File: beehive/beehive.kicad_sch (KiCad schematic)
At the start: 23 parts, among them J1 M05PTH, Q1 MMBT4403, U1 ESP32-S3-WROOM-1U, U2 HX711, U3 ADXL362

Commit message: added custom library submodule
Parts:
- C1, C2, C3, C4, C5: footprint SparkFun_HX711_Load_Cell:0603-CAP -> Board_SparkFun_HX711_Load_Cell:0603-CAP
- C6, C7: footprint SparkFun_HX711_Load_Cell:1210 -> Board_SparkFun_HX711_Load_Cell:1210
- C8: footprint ADXL362 BOB v01:0402-CAP -> Board_ADXL362_BOB_v01:0402-CAP
- J1, JP4: footprint SparkFun_HX711_Load_Cell:1X05 -> Board_SparkFun_HX711_Load_Cell:1X05
- JP1: footprint ADXL362 BOB v01:1X04 -> Board_ADXL362_BOB_v01:1X04
- JP2: footprint SparkFun_HX711_Load_Cell:1X02 -> Board_SparkFun_HX711_Load_Cell:1X02
- L1: footprint SparkFun_HX711_Load_Cell:0805 -> Board_SparkFun_HX711_Load_Cell:0805
- Q1: footprint SparkFun_HX711_Load_Cell:SOT23-3 -> Board_SparkFun_HX711_Load_Cell:SOT23-3
- R1, R2, R3, R4, R5: footprint SparkFun_HX711_Load_Cell:0603-RES -> Board_SparkFun_HX711_Load_Cell:0603-RES
- SJ2: footprint SparkFun_HX711_Load_Cell:PAD-JUMPER-2-NC_BY_TRACE_YES_SILK -> Board_SparkFun_HX711_Load_Cell:PAD-JUMPER-2-NC_BY_TRACE_YES_SILK
- U1: footprint ESP32:XCVR_ESP32-S3-WROOM-1U -> ESP32-S3-WROOM-1:XCVR_ESP32-S3-WROOM-1U
- U3: footprint adxl362:LGA-16-3X2.5 -> ADXL362:LGA-16-3X2.5
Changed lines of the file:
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@@
 			)
 		)
-		(property "Footprint" "SparkFun_HX711_Load_Cell:1X02"
+		(property "Footprint" "Board_SparkFun_HX711_Load_Cell:1X02"
 			(at 217.17 74.93 0)
 			(effects
@@
 			)
 		)
-		(property "Footprint" "SparkFun_HX711_Load_Cell:0603-CAP"
+		(property "Footprint" "Board_SparkFun_HX711_Load_Cell:0603-CAP"
 			(at 250.19 29.21 0)
 			(effects
@@
 			)
 		)
-		(property "Footprint" "SparkFun_HX711_Load_Cell:0805"
+		(property "Footprint" "Board_SparkFun_HX711_Load_Cell:0805"
 			(at 273.05 49.53 0)
 			(effects
@@
 			)
 		)
-		(property "Footprint" "SparkFun_HX711_Load_Cell:0603-CAP"
+		(property "Footprint" "Board_SparkFun_HX711_Load_Cell:0603-CAP"
 			(at 247.65 57.15 0)
 			(effects
@@
 			)
 		)
-		(property "Footprint" "SparkFun_HX711_Load_Cell:SOT23-3"
+		(property "Footprint" "Board_SparkFun_HX711_Load_Cell:SOT23-3"
 			(at 293.37 41.91 0)
 			(effects
@@
 			)
 		)
-		(property "Footprint" "SparkFun_HX711_Load_Cell:0603-RES"
+		(property "Footprint" "Board_SparkFun_HX711_Load_Cell:0603-RES"
 			(at 285.75 72.39 0)
 			(effects
@@
 			)
 		)
-		(property "Footprint" "SparkFun_HX711_Load_Cell:0603-CAP"
+		(property "Footprint" "Board_SparkFun_HX711_Load_Cell:0603-CAP"
 			(at 295.91 97.79 0)
 			(effects
@@
 			)
 		)
-		(property "Footprint" "SparkFun_HX711_Load_Cell:1X05"
+		(property "Footprint" "Board_SparkFun_HX711_Load_Cell:1X05"
 			(at 217.17 54.61 0)
 			(effects
@@
 			)
 		)
-		(property "Footprint" "SparkFun_HX711_Load_Cell:0603-RES"
+		(property "Footprint" "Board_SparkFun_HX711_Load_Cell:0603-RES"
 			(at 285.75 57.15 0)
 			(effects
@@
 			)
 		)
-		(property "Footprint" "ADXL362 BOB v01:0402-CAP"
+		(property "Footprint" "Board_ADXL362_BOB_v01:0402-CAP"
 			(at 353.06 201.93 0)
 			(effects
@@
 			)
 		)
-		(property "Footprint" "SparkFun_HX711_Load_Cell:0603-RES"
+		(property "Footprint" "Board_SparkFun_HX711_Load_Cell:0603-RES"
 			(at 288.29 102.87 0)
 			(effects
@@
 			)
 		)
-		(property "Footprint" "SparkFun_HX711_Load_Cell:0603-RES"
+		(property "Footprint" "Board_SparkFun_HX711_Load_Cell:0603-RES"
 			(at 288.29 90.17 0)
 			(effects
@@
 			)
 		)
-		(property "Footprint" "ESP32:XCVR_ESP32-S3-WROOM-1U"
+		(property "Footprint" "ESP32-S3-WROOM-1:XCVR_ESP32-S3-WROOM-1U"
 			(at 45.72 74.93 0)
 			(effects
@@
 			)
 		)
-		(property "Footprint" "SparkFun_HX711_Load_Cell:0603-RES"
+		(property "Footprint" "Board_SparkFun_HX711_Load_Cell:0603-RES"
 			(at 351.79 39.37 0)
 			(effects
@@
 			)
 		)
-		(property "Footprint" "SparkFun_HX711_Load_Cell:0603-CAP"
+		(property "Footprint" "Board_SparkFun_HX711_Load_Cell:0603-CAP"
 			(at 298.45 80.01 0)
 			(effects
@@
 			)
 		)
-		(property "Footprint" "ADXL362 BOB v01:1X04"
+		(property "Footprint" "Board_ADXL362_BOB_v01:1X04"
 			(at 312.42 161.29 0)
 			(effects
@@
 			)
 		)
-		(property "Footprint" "SparkFun_HX711_Load_Cell:0603-CAP"
+		(property "Footprint" "Board_SparkFun_HX711_Load_Cell:0603-CAP"
 			(at 262.89 29.21 0)
 			(effects
@@
 			)
 		)
-		(property "Footprint" "SparkFun_HX711_Load_Cell:1210"
+		(property "Footprint" "Board_SparkFun_HX711_Load_Cell:1210"
 			(at 278.13 29.21 0)
 			(effects
@@
 			)
 		)
-		(property "Footprint" "SparkFun_HX711_Load_Cell:1X05"
+		(property "Footprint" "Board_SparkFun_HX711_Load_Cell:1X05"
 			(at 379.73 69.85 0)
 			(effects
@@
 			)
 		)
-		(property "Footprint" "adxl362:LGA-16-3X2.5"
+		(property "Footprint" "ADXL362:LGA-16-3X2.5"
 			(at 316.23 196.85 0)
 			(effects
@@
 			)
 		)
-		(property "Footprint" "SparkFun_HX711_Load_Cell:1210"
+		(property "Footprint" "Board_SparkFun_HX711_Load_Cell:1210"
 			(at 257.81 57.15 0)
 			(effects
@@
 			)
 		)
-		(property "Footprint" "SparkFun_HX711_Load_Cell:PAD-JUMPER-2-NC_BY_TRACE_YES_SILK"
+		(property "Footprint" "Board_SparkFun_HX711_Load_Cell:PAD-JUMPER-2-NC_BY_TRACE_YES_SILK"
 			(at 351.79 54.61 0)
 			(effects

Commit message: TP5100 and ESP32 remaining
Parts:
- removed JP1: M04PTH, Board_ADXL362_BOB_v01:1X04, symbol ADXL362 BOB v01-eagle-import:M04PTH
- added C10, C9: 10uF/25V, Capacitor_SMD:C_0603_1608Metric_Pad1.08x0.95mm_HandSolder, symbol Device:C
- added C11: 0.1uF, symbol Device:C
- added C12: 3.9nF, symbol Device:C
- added C13, C14: 22uF/6.3V, symbol Device:C
- added C15: 10nF, symbol Device:C
- added C16, C17: 1uF, symbol Device:C
- added IC1: MP2307, MP2307:SO8-TH, symbol MP2307:MP2307
- added J2, J3: Conn_01x04_Pin, Connector_JST:JST_XH_B4B-XH-A_1x04_P2.50mm_Vertical, symbol Connector:Conn_01x04_Pin
- added J4: Conn_01x07_Socket, Connector_JST:JST_XH_B7B-XH-A_1x07_P2.50mm_Vertical, symbol Connector:Conn_01x07_Socket
- added J5: Conn_01x04_Pin, symbol Connector:Conn_01x04_Pin
- added J6: Screw_Terminal_01x07, symbol Connector:Screw_Terminal_01x07
- added J7, J8: Conn_01x03_Pin, symbol Connector:Conn_01x03_Pin
- added L2: 10uH/4A, symbol Device:L
- added R6: 100k, symbol Device:R_US
- added R7: 6.8k, symbol Device:R_US
- added R8: 28.7k/1%, symbol Device:R_US
- added R9: 10k/1%, symbol Device:R_US
- added U5: TP5100, TP5100:QFN65P400X400X90-17N, symbol TP5100:TP5100
- added U6: MCP1700x-330xxTT, Package_TO_SOT_SMD:SOT-23, symbol Regulator_Linear:MCP1700x-330xxTT
- C1, C2, C3, C4, C5: symbol SparkFun_HX711_Load_Cell-eagle-import:0.1UF-25V-5%(0603) -> Board_SparkFun_HX711_Load_Cell:0.1UF-25V-5%(0603)
- C8: value .1uF -> 0.1uF; symbol ADXL362 BOB v01-eagle-import:CAP0402-CAP -> Board_SparkFun_HX711_Load_Cell:0.1UF-25V-5%(0603)
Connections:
- net 3.3V is gone; now on net +3.3V: C8.2
- net GND: now also U3.P$12 (GND), U3.P$13 (GND), U3.P$16 (GND), C10.2, C11.2, C13.2, C14.1, C16.2, C17.2, C9.2, IC1.4 (GND), J2.2 (Pin_2), J4.2 (Pin_2), J5.2 (Pin_2), J8.1 (Pin_1), L2.2, R7.1, R9.2
- net SCK: now also J4.4 (Pin_4), J7.3 (Pin_3)
- net +3.3V: now reaches U3.P$1 (VDDIO)
- net +3.3V: now also U3.P$14 (VS), C16.1, J2.1 (Pin_1), J4.1 (Pin_1), J5.1 (Pin_1), J8.2 (Pin_2), U6.2 (VO)
- net at U3.P$11 (INT1): now also J2.3 (Pin_3)
- net at U3.P$4 (SCLK): now also J3.4 (Pin_4)
- net at U3.P$6 (MOSI): now also J3.3 (Pin_3)
- net at U3.P$7 (MISO): now also J3.2 (Pin_2)
- net at U3.P$8 (~{CS}): now also J3.1 (Pin_1)
- net at U3.P$9 (INT2): now also J2.4 (Pin_4)
- new net: C12.1, IC1.6 (COMP)
- new net: C12.2, R7.2
- new net: C13.1, C14.2, R8.1
- new net: C15.2, C17.1, IC1.3 (SW), L2.1, U6.3 (VI)
- new net: C11.1, IC1.8 (SS)
- new net: C15.1, IC1.1 (BS)
- new net: IC1.5 (FB), R8.2, R9.1
- new net: IC1.7 (EN), R6.2
- new net: U5.1 (VIN), U5.16 (VIN), U5.4 (VIN), U5.5 (VIN)
- new net: U5.2 (LX), U5.3 (LX)
- new net +BATT: C10.1, C9.1, IC1.2 (IN), R6.1
- new net SCL: J4.6 (Pin_6), J5.3 (Pin_3)
- new net SD: J4.3 (Pin_3), J8.3 (Pin_3)
- new net SDA: J4.7 (Pin_7), J5.4 (Pin_4)
- new net WS: J4.5 (Pin_5), J7.2 (Pin_2)
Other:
- note added: "BME280"
- note added: "INMP441"
- moved on the sheet: C8, U1, U3

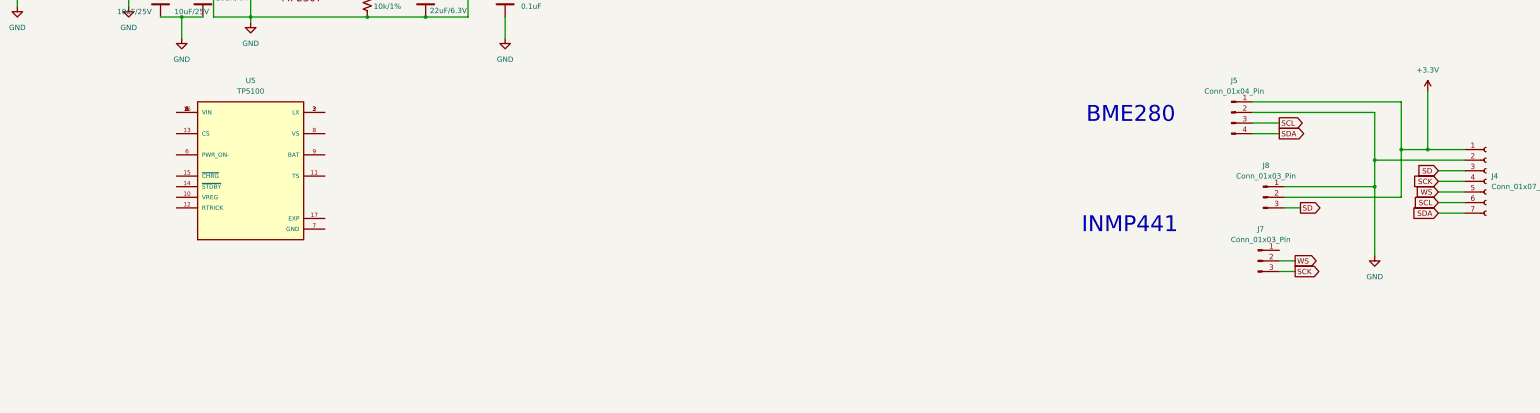
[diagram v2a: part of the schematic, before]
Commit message: change connection from the sensor block
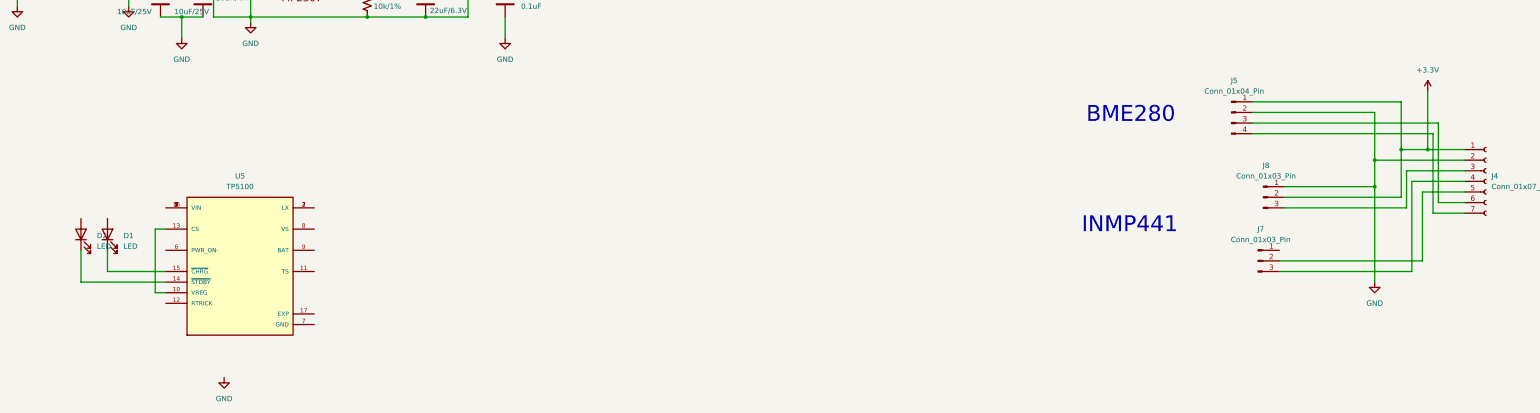
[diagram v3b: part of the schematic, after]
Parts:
- added D1, D2: LED, symbol Device:LED
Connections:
- net SCK: no longer J4.4 (Pin_4), J7.3 (Pin_3)
- net at U5.10 (VREG): now also U5.13 (CS)
- net at U5.14 (~{STDBY}): now also D2.1 (K)
- net at U5.15 (~{CHRG}): now also D1.1 (K)
- net SCL: no longer names the net of J4.6 (Pin_6), J5.3 (Pin_3)
- net SD: no longer names the net of J4.3 (Pin_3), J8.3 (Pin_3)
- net SDA: no longer names the net of J4.7 (Pin_7), J5.4 (Pin_4)
- net WS: no longer names the net of J4.5 (Pin_5), J7.2 (Pin_2)
- new net: J4.4 (Pin_4), J7.3 (Pin_3)
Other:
- moved on the sheet: U5

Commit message: 123
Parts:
- removed J1: M05PTH, Board_SparkFun_HX711_Load_Cell:1X05, symbol SparkFun_HX711_Load_Cell-eagle-import:M05PTH
- removed J3: Conn_01x04_Pin, Connector_JST:JST_XH_B4B-XH-A_1x04_P2.50mm_Vertical, symbol Connector:Conn_01x04_Pin
- added BT1: Battery, symbol Device:Battery
- added C18, C19, C22, C24, C26, C27, C28: 0.1uF, symbol Device:C
- added C20, C21, C23, C25: 10uF, Capacitor_SMD:C_0603_1608Metric_Pad1.08x0.95mm_HandSolder, symbol Device:C
- added J9: USB_C_Receptacle_USB2.0_16P, symbol Connector:USB_C_Receptacle_USB2.0_16P
- added L3: 22uH/2A, symbol Device:L
- added R10: 1k, symbol Device:R_US
- added R11: 0.1, symbol Device:R_US
- added R12: 10k, Board_SparkFun_HX711_Load_Cell:0603-RES, symbol SparkFun_HX711_Load_Cell-eagle-import:20KOHM1/10W1%(0603)
- added R13: 100, Board_SparkFun_HX711_Load_Cell:0603-RES, symbol SparkFun_HX711_Load_Cell-eagle-import:20KOHM1/10W1%(0603)
- added R14, R15: 5.1k, Resistor_SMD:R_0805_2012Metric_Pad1.20x1.40mm_HandSolder, symbol SparkFun_HX711_Load_Cell-eagle-import:20KOHM1/10W1%(0603)
- added R16, R17: 4.7k, Board_SparkFun_HX711_Load_Cell:0603-RES, symbol SparkFun_HX711_Load_Cell-eagle-import:20KOHM1/10W1%(0603)
- added SW1, SW2: SW_Push, symbol Switch:SW_Push
- D1: value LED -> LED red
- D2: value LED -> LED green
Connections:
- net DAT is gone; now on net IO4_DOUT: U2.12 (DOUT)
- net SCK is gone; now on net IO3_PD_SCK: U2.11 (PD_SCK)
- net +3.3V: now also J6.1 (Pin_1), U1.2 (3V3), C25.1, C26.1, R12.1, R16.2, R17.2
- net GND: now also J6.2 (Pin_2), U1.1 (GND), U1.40 (GND), U1.41_1 (GND), U1.41_2 (GND), U1.41_3 (GND), U1.41_4 (GND), U1.41_5 (GND), U1.41_6 (GND), U1.41_7 (GND), U1.41_8 (GND), U1.41_9 (GND), U5.11 (TS), U5.17 (EXP), U5.7 (GND), C18.2, C19.2, C20.2, C21.2, C22.2, C23.2, C24.2, C25.2, C26.2, C27.2, C28.2, J9.A1 (GND), J9.A12 (GND), J9.B1 (GND), J9.B12 (GND), J9.S1 (SHIELD), R14.2, R15.2, SW1.2, SW2.2
- net IO10_CS: now reaches U3.P$8 (~{CS})
- net IO10_CS: now also U1.18 (IO10)
- net IO13_MISO: now reaches U3.P$7 (MISO)
- net IO13_MISO: now also U1.21 (IO13)
- net IO11_MOSI: now reaches U3.P$6 (MOSI)
- net IO11_MOSI: now also U1.19 (IO11)
- net IO12_SCLK: now reaches U3.P$4 (SCLK)
- net IO12_SCLK: now also U1.20 (IO12)
- net INMP_SD: now reaches J4.3 (Pin_3), J8.3 (Pin_3)
- net INMP_WS: now reaches J4.5 (Pin_5), J7.2 (Pin_2)
- net INMP_SCK: now reaches J4.4 (Pin_4), J7.3 (Pin_3)
- net at D2.2 (A): now also D1.2 (A), R10.2
- net IO8_SDA: now reaches U1.12 (IO8)
- net IO8_SDA: now also J6.7 (Pin_7), R17.1
- net D-: now reaches U1.13 (IO19)
- net D-: now also J9.A7 (D-), J9.B7 (D-)
- net D+: now reaches U1.14 (IO20)
- net D+: now also J9.A6 (D+), J9.B6 (D+)
- net IO3_PD_SCK: now reaches U1.15 (IO3)
- net IO9_SCL: now reaches U1.17 (IO9)
- net IO9_SCL: now also J6.6 (Pin_6), R16.1
- net BOOT: now reaches U1.27 (IO0)
- net BOOT: now also R13.1
- net EN: now reaches U1.3 (EN)
- net EN: now also C27.1, C28.1, R12.2, SW1.1
- net IO4_DOUT: now reaches U1.4 (IO4)
- net IO5_SD: now reaches U1.5 (IO5)
- net IO5_SD: now also J6.3 (Pin_3)
- net IO6_WS: now reaches U1.6 (IO6)
- net IO6_WS: now also J6.4 (Pin_4)
- net IO7_SCK: now reaches U1.7 (IO7)
- net IO7_SCK: now also J6.5 (Pin_5)
- net +12V: now reaches U5.1 (VIN), U5.16 (VIN), U5.4 (VIN), U5.5 (VIN)
- net +12V: now also C19.1, C20.1, R10.1
- net at U5.10 (VREG), U5.13 (CS): now also U5.12 (RTRICK), BT1.2 (-), C18.1
- net at U5.2 (LX), U5.3 (LX): now also L3.1
- net at U5.8 (VS): now also C23.1, C24.1, L3.2, R11.1
- net at U5.9 (BAT): now also BT1.1 (+), C21.1, C22.1
- net BME_SCL: now reaches J4.6 (Pin_6), J5.3 (Pin_3)
- net BME_SDA: now reaches J4.7 (Pin_7), J5.4 (Pin_4)
- new net: J9.A5 (CC1), R14.1
- new net: J9.B5 (CC2), R15.1
- new net: R13.2, SW2.1
- new net +5V: J9.A4 (VBUS), J9.A9 (VBUS), J9.B4 (VBUS), J9.B9 (VBUS)
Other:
- note removed: "IO: 2.7-5.5V"
- note removed: "VCC: 2.7-5.5V"
- note removed: "VDD: 2.7-5.5V"
- moved on the sheet: C1, C10, C11, C12, C13, C14, C15, C16, C17, C2, C3, C4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

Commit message: last
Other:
- note added: "HX711"
- moved on the sheet: C10, C11, C12, C13, C14, C15, C16, C17, C9, IC1, L2, R6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
